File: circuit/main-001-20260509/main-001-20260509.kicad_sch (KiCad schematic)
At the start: 1 part, among them U1 DEV-16771

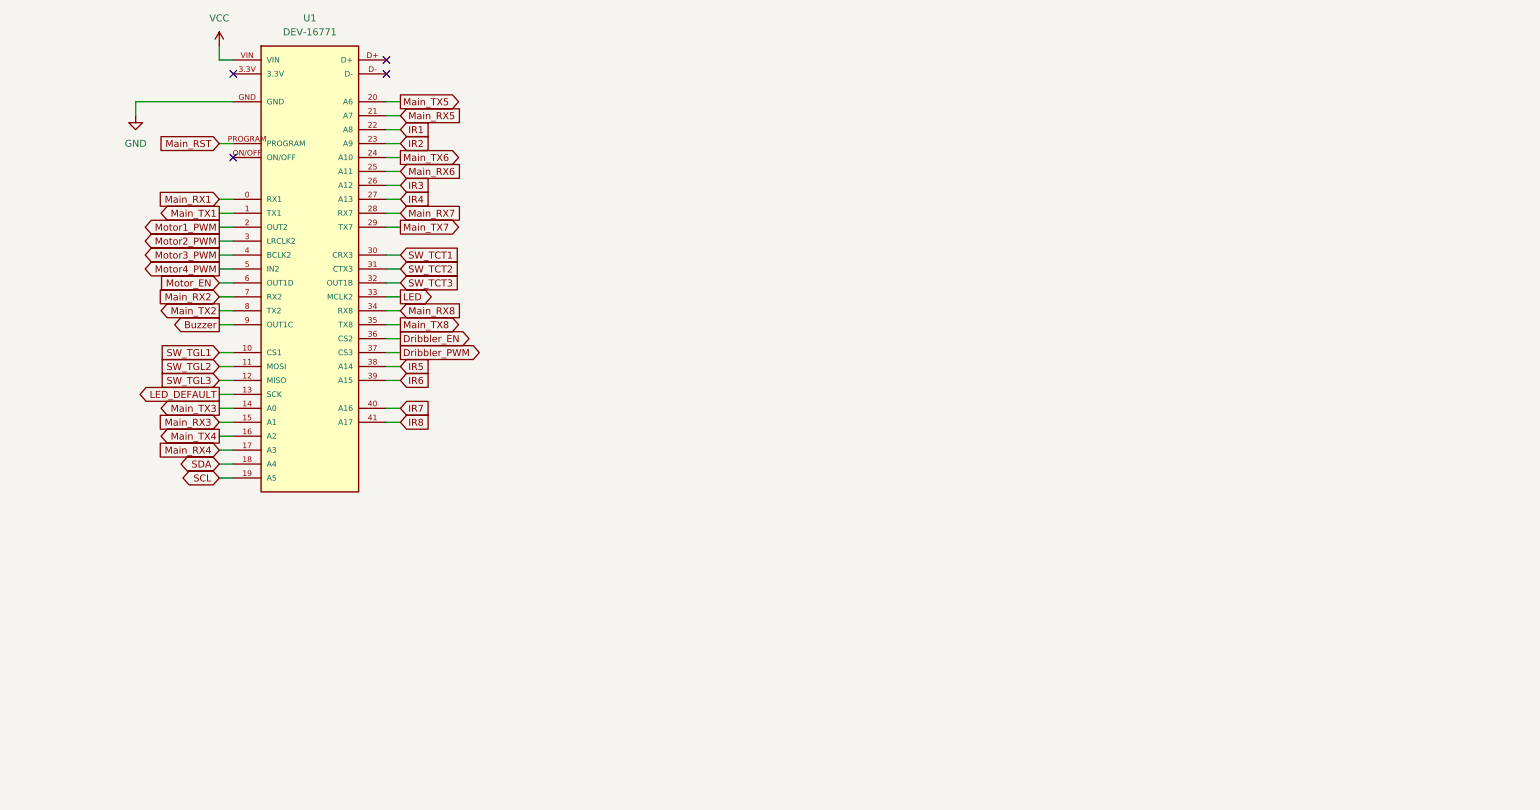
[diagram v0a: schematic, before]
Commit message: Update メイン基板の回路を進めた
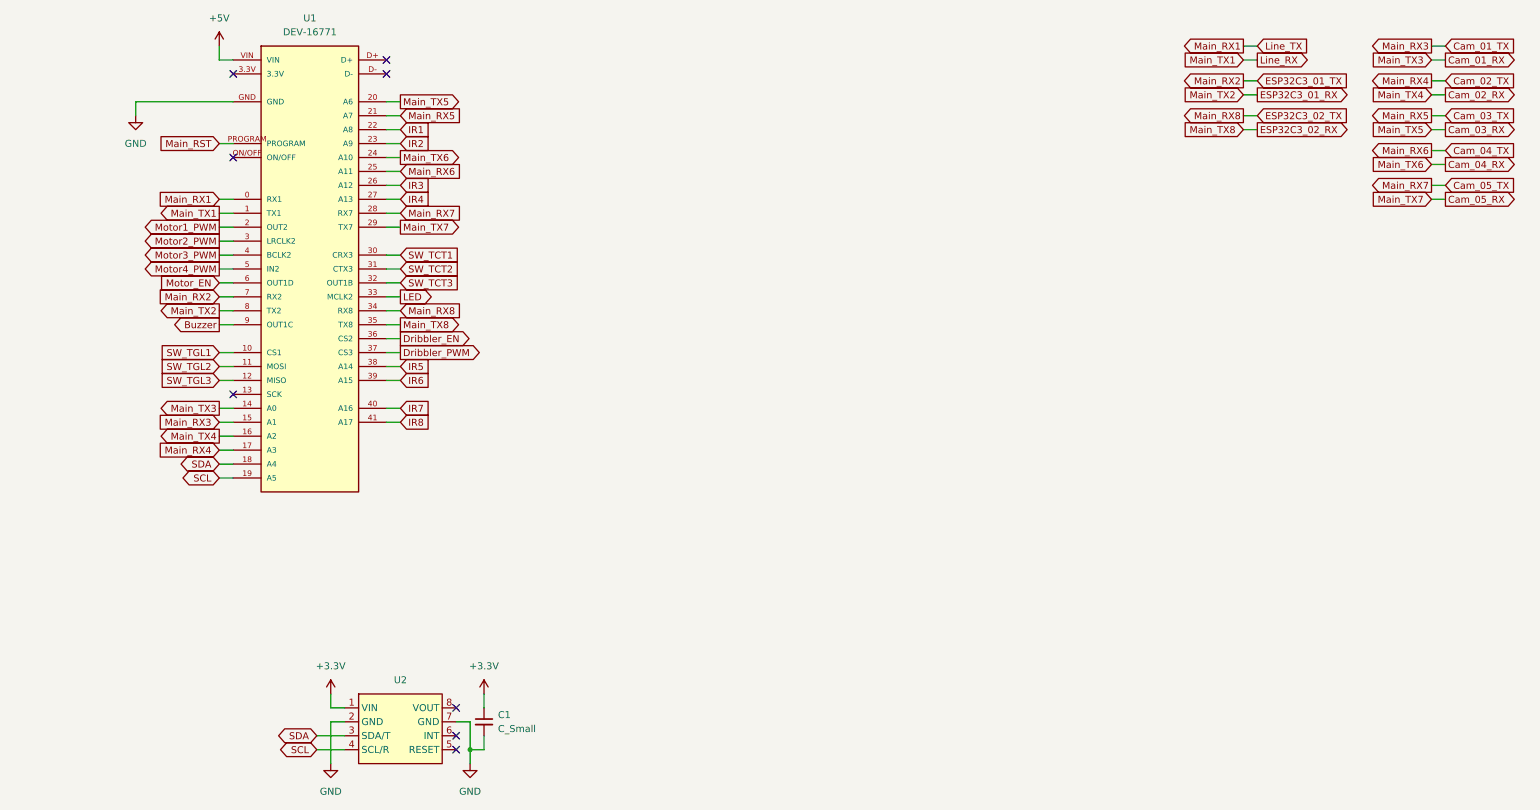
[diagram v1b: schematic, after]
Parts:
- added C1: C_Small, symbol Device:C_Small
- added U2: (no value), symbol @Thrive_symbol_main:BNO055
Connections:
- net GND: now also C1.2, U2.2 (GND), U2.7 (GND)
- net SCL: now also U2.4 (SCL/R)
- net SDA: now also U2.3 (SDA/T)
- net LED_DEFAULT: no longer names the net of U1.13 (SCK)
- net Main_RX1 renamed Line_TX
- net Main_RX2 renamed ESP32C3_01_TX
- net Main_RX3 renamed Cam_01_TX
- net Main_RX4 renamed Cam_02_TX
- net Main_RX5 renamed Cam_03_TX
- net Main_RX6 renamed Cam_04_TX
- net Main_RX7 renamed Cam_05_TX
- net Main_RX8 renamed ESP32C3_02_TX
- net Main_TX1 renamed Line_RX
- net Main_TX2 renamed ESP32C3_01_RX
- net Main_TX3 renamed Cam_01_RX
- net Main_TX4 renamed Cam_02_RX
- net Main_TX5 renamed Cam_03_RX
- net Main_TX6 renamed Cam_04_RX
- net Main_TX7 renamed Cam_05_RX
- net Main_TX8 renamed ESP32C3_02_RX
- net VCC renamed +5V
- new net +3.3V: C1.1, U2.1 (VIN)
- no-connect marks 4 -> 8

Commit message: Update メイン基板ほぼアップデートなし
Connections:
- net Line_TX: no longer U1.0 (RX1)
- new net RX1_{teensy}-TX_{Arduino}: U1.0 (RX1)
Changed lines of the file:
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@@
 		)
 	)
-	(global_label "Main_RX1"
+	(global_label "RX1_{teensy}-TX_{Arduino}"
 		(shape input)
 		(at 38.1 53.34 180)
@@
 		)
 		(property "Intersheetrefs" "${INTERSHEET_REFS}"
-			(at 25.8604 53.34 0)
+			(at 17.1268 53.34 0)
 			(hide yes)
 			(show_name no)

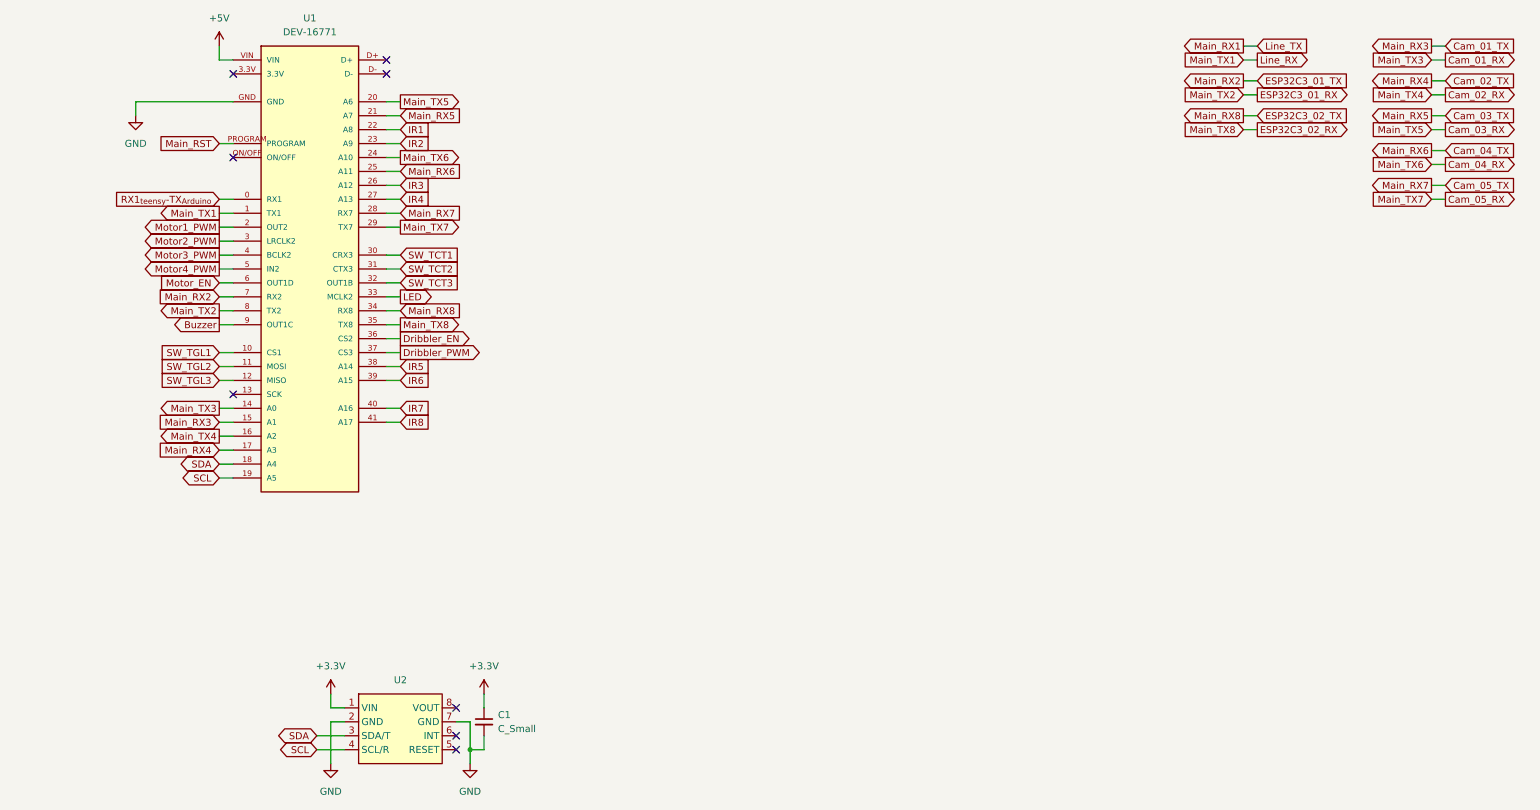
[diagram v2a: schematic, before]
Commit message: Update メイン基板はピン関連とレベル変換、サブ基板はESP周りを追加した
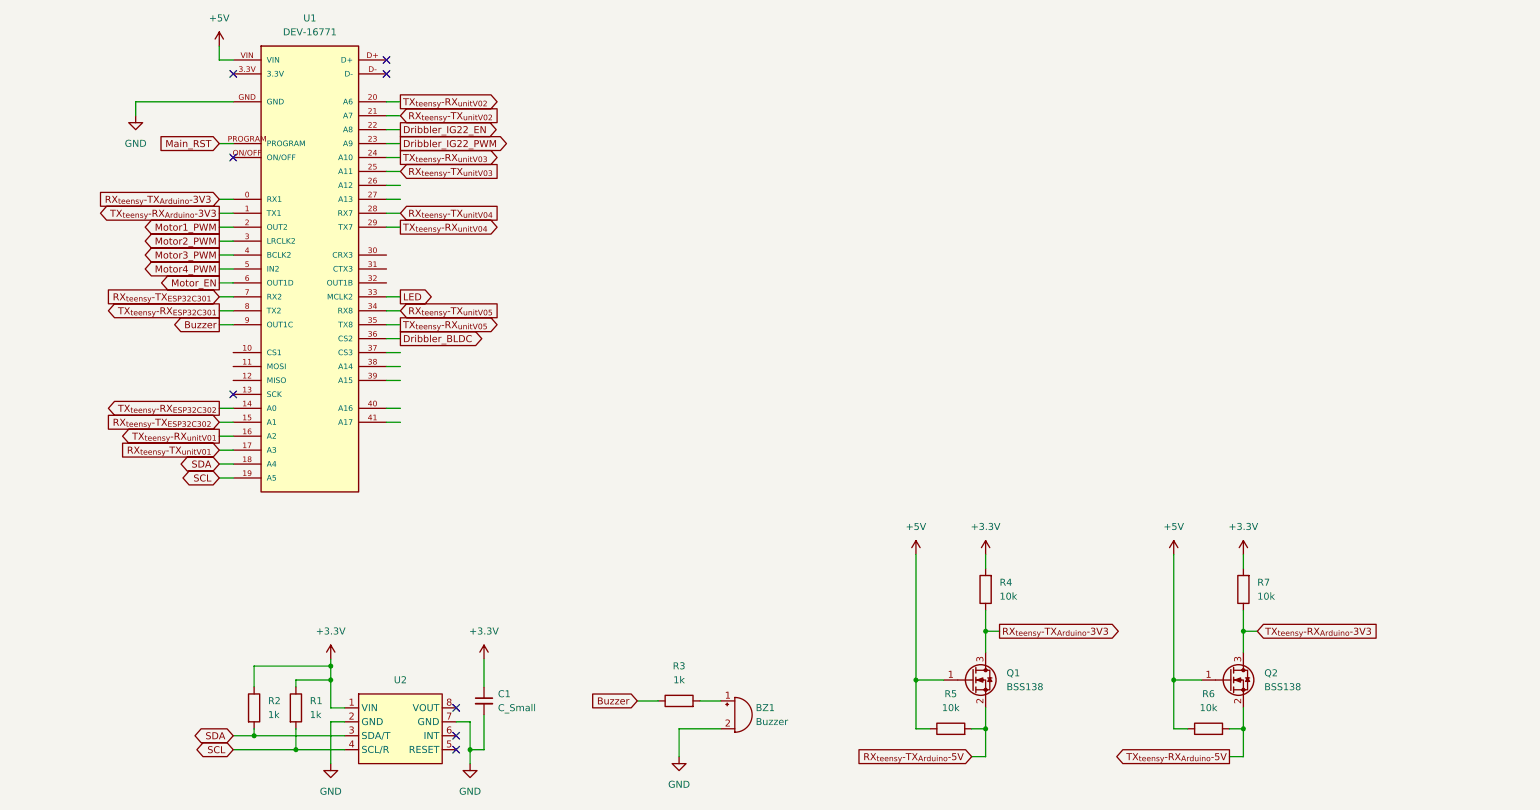
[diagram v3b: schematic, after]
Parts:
- added BZ1: Buzzer, symbol Device:Buzzer
- added Q1, Q2: BSS138, Package_TO_SOT_SMD:SOT-23, symbol Transistor_FET:BSS138
- added R1, R2, R3: 1k, symbol Device:R
- added R4, R5, R6, R7: 10k, symbol Device:R
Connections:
- net +3.3V: now also R1.1, R2.1, R4.2, R7.2
- net +5V: now also Q1.1 (G), Q2.1 (G), R5.1, R6.1
- net Buzzer: now also R3.1
- net GND: now also BZ1.2 (-)
- net SCL: now also R1.2
- net SDA: now also R2.2
- net Cam_01_RX renamed TX_{teensy}-RX_{ESP32C302}
- net Cam_01_TX renamed RX_{teensy}-TX_{ESP32C302}
- net Cam_02_RX renamed TX_{teensy}-RX_{unitV01}
- net Cam_02_TX renamed RX_{teensy}-TX_{unitV01}
- net Cam_03_RX renamed TX_{teensy}-RX_{unitV02}
- net Cam_03_TX renamed RX_{teensy}-TX_{unitV02}
- net Cam_04_RX renamed TX_{teensy}-RX_{unitV03}
- net Cam_04_TX renamed RX_{teensy}-TX_{unitV03}
- net Cam_05_RX renamed TX_{teensy}-RX_{unitV04}
- net Cam_05_TX renamed RX_{teensy}-TX_{unitV04}
- net Dribbler_EN renamed Dribbler_BLDC
- net Dribbler_PWM: no longer names the net of U1.37 (CS3)
- net ESP32C3_01_RX renamed TX_{teensy}-RX_{ESP32C301}
- net ESP32C3_01_TX renamed RX_{teensy}-TX_{ESP32C301}
- net ESP32C3_02_RX renamed TX_{teensy}-RX_{unitV05}
- net ESP32C3_02_TX renamed RX_{teensy}-TX_{unitV05}
- net IR1 renamed Dribbler_IG22_EN
- net IR2 renamed Dribbler_IG22_PWM
- net IR3: no longer names the net of U1.26 (A12)
- net IR4: no longer names the net of U1.27 (A13)
- net IR5: no longer names the net of U1.38 (A14)
- net IR6: no longer names the net of U1.39 (A15)
- net IR7: no longer names the net of U1.40 (A16)
- net IR8: no longer names the net of U1.41 (A17)
- net Line_RX renamed TX_{teensy}-RX_{Arduino}-3V3
- net TX_{teensy}-RX_{Arduino}-3V3: now also Q2.3 (D), R7.1
- net RX1_{teensy}-TX_{Arduino} renamed RX_{teensy}-TX_{Arduino}-3V3
- net RX_{teensy}-TX_{Arduino}-3V3: now also Q1.3 (D), R4.1
- net SW_TCT1: no longer names the net of U1.30 (CRX3)
- net SW_TCT2: no longer names the net of U1.31 (CTX3)
- net SW_TCT3: no longer names the net of U1.32 (OUT1B)
- net SW_TGL1: no longer names the net of U1.10 (CS1)
- net SW_TGL2: no longer names the net of U1.11 (MOSI)
- net SW_TGL3: no longer names the net of U1.12 (MISO)
- new net: BZ1.1 (+), R3.2
- new net RX_{teensy}-TX_{Arduino}-5V: Q1.2 (S), R5.2
- new net TX_{teensy}-RX_{Arduino}-5V: Q2.2 (S), R6.2
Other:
- moved on the sheet: C1

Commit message: Create ネオピクセル基板完成した
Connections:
- net ballcatchsig_front: now reaches U1.10 (CS1)
- net ballcatchsig_back: now reaches U1.11 (MOSI)
- net SW_TCT: now reaches U1.12 (MISO)
- net RX_{teensy}-TX_{unitV01} renamed RX_{teensy}-TX_{unitV1}
- net RX_{teensy}-TX_{unitV02} renamed RX_{teensy}-TX_{unitV2}
- net RX_{teensy}-TX_{unitV03} renamed RX_{teensy}-TX_{unitV3}
- net RX_{teensy}-TX_{unitV04} renamed RX_{teensy}-TX_{unitV4}
- net RX_{teensy}-TX_{unitV05} renamed RX_{teensy}-TX_{unitV5}
- net TX_{teensy}-RX_{unitV01} renamed TX_{teensy}-RX_{unitV1}
- net TX_{teensy}-RX_{unitV02} renamed TX_{teensy}-RX_{unitV2}
- net TX_{teensy}-RX_{unitV03} renamed TX_{teensy}-RX_{unitV3}
- net TX_{teensy}-RX_{unitV04} renamed TX_{teensy}-RX_{unitV4}
- net TX_{teensy}-RX_{unitV05} renamed TX_{teensy}-RX_{unitV5}
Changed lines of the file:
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@@
+	(wire
+		(pts
+			(xy 38.1 83.82) (xy 40.64 83.82)
+		)
+		(stroke
+			(width 0)
+			(type default)
+		)
+	)
 	(wire
 		(pts
@@
 	(wire
 		(pts
+			(xy 38.1 81.28) (xy 40.64 81.28)
+		)
+		(stroke
+			(width 0)
+			(type default)
+		)
+	)
+	(wire
+		(pts
+			(xy 38.1 86.36) (xy 40.64 86.36)
+		)
+		(stroke
+			(width 0)
+			(type default)
+		)
+	)
+	(wire
+		(pts
 			(xy 52.07 142.24) (xy 52.07 140.97)
 		)
@@
 		)
 	)
-	(global_label "RX_{teensy}-TX_{unitV05}"
+	(global_label "RX_{teensy}-TX_{unitV5}"
 		(shape input)
 		(at 71.12 73.66 0)
@@
 		)
 		(property "Intersheetrefs" "${INTERSHEET_REFS}"
-			(at 90.9321 73.66 0)
+			(at 89.9645 73.66 0)
 			(hide yes)
 			(show_name no)
@@
 		)
 	)
+	(global_label "ballcatchsig_back"
+		(shape input)
+		(at 38.1 83.82 180)
+		(fields_autoplaced yes)
+		(effects
+			(font
+				(size 1.27 1.27)
+			)
+			(justify right)
+		)
+		(property "Intersheetrefs" "${INTERSHEET_REFS}"
+			(at 18.1213 83.82 0)
+			(hide yes)
+			(show_name no)
+			(do_not_autoplace no)
+			(effects
+				(font
+					(size 1.27 1.27)
+				)
+				(justify right)
+			)
+		)
+	)
 	(global_label "Motor3_PWM"
 		(shape output)
@@
 		)
 	)
+	(global_label "ballcatchsig_front"
+		(shape input)
+		(at 38.1 81.28 180)
+		(fields_autoplaced yes)
+		(effects
+			(font
+				(size 1.27 1.27)
+			)
+			(justify right)
+		)
+		(property "Intersheetrefs" "${INTERSHEET_REFS}"
+			(at 18.0004 81.28 0)
+			(hide yes)
+			(show_name no)
+			(do_not_autoplace no)
+			(effects
+				(font
+					(size 1.27 1.27)
+				)
+				(justify right)
+			)
+		)
+	)
 	(global_label "RX_{teensy}-TX_{ESP32C301}"
 		(shape input)
@@
 		)
 	)
-	(global_label "RX_{teensy}-TX_{unitV02}"
+	(global_label "RX_{teensy}-TX_{unitV2}"
 		(shape input)
 		(at 71.12 38.1 0)
@@
 		)
 		(property "Intersheetrefs" "${INTERSHEET_REFS}"
-			(at 90.9321 38.1 0)
+			(at 89.9645 38.1 0)
 			(hide yes)
 			(show_name no)
@@
 		)
 	)
-	(global_label "RX_{teensy}-TX_{unitV03}"
+	(global_label "RX_{teensy}-TX_{unitV3}"
 		(shape input)
 		(at 71.12 48.26 0)
@@
 		)
 		(property "Intersheetrefs" "${INTERSHEET_REFS}"
-			(at 90.9321 48.26 0)
+			(at 89.9645 48.26 0)
 			(hide yes)
 			(show_name no)
@@
 		)
 	)
-	(global_label "RX_{teensy}-TX_{unitV01}"
+	(global_label "RX_{teensy}-TX_{unitV1}"
 		(shape input)
 		(at 38.1 99.06 180)
@@
 		)
 		(property "Intersheetrefs" "${INTERSHEET_REFS}"
-			(at 18.2879 99.06 0)
+			(at 19.2555 99.06 0)
 			(hide yes)
 			(show_name no)
@@
 		)
 	)
-	(global_label "RX_{teensy}-TX_{unitV04}"
+	(global_label "RX_{teensy}-TX_{unitV4}"
 		(shape input)
 		(at 71.12 55.88 0)
@@
 		)
 		(property "Intersheetrefs" "${INTERSHEET_REFS}"
-			(at 90.9321 55.88 0)
+			(at 89.9645 55.88 0)
 			(hide yes)
 			(show_name no)
@@
 		)
 	)
-	(global_label "TX_{teensy}-RX_{unitV05}"
+	(global_label "TX_{teensy}-RX_{unitV5}"
 		(shape output)
 		(at 71.12 76.2 0)
@@
 		)
 		(property "Intersheetrefs" "${INTERSHEET_REFS}"
-			(at 90.9321 76.2 0)
+			(at 89.9645 76.2 0)
 			(hide yes)
 			(show_name no)
@@
 		)
 	)
-	(global_label "TX_{teensy}-RX_{unitV01}"
+	(global_label "TX_{teensy}-RX_{unitV1}"
 		(shape output)
 		(at 38.1 96.52 180)
@@
 		)
 		(property "Intersheetrefs" "${INTERSHEET_REFS}"
-			(at 18.2879 96.52 0)
+			(at 19.2555 96.52 0)
 			(hide yes)
 			(show_name no)
@@
 		)
 	)
-	(global_label "TX_{teensy}-RX_{unitV04}"
+	(global_label "TX_{teensy}-RX_{unitV4}"
 		(shape output)
 		(at 71.12 58.42 0)
@@
 		)
 		(property "Intersheetrefs" "${INTERSHEET_REFS}"
-			(at 90.9321 58.42 0)
+			(at 89.9645 58.42 0)
 			(hide yes)
 			(show_name no)
@@
 		)
 	)
-	(global_label "TX_{teensy}-RX_{unitV03}"
+	(global_label "TX_{teensy}-RX_{unitV3}"
 		(shape output)
 		(at 71.12 45.72 0)
@@
 		)
 		(property "Intersheetrefs" "${INTERSHEET_REFS}"
-			(at 90.9321 45.72 0)
+			(at 89.9645 45.72 0)
 			(hide yes)
 			(show_name no)
@@
 		)
 	)
-	(global_label "TX_{teensy}-RX_{unitV02}"
+	(global_label "TX_{teensy}-RX_{unitV2}"
 		(shape output)
 		(at 71.12 35.56 0)
@@
 		)
 		(property "Intersheetrefs" "${INTERSHEET_REFS}"
-			(at 90.9321 35.56 0)
+			(at 89.9645 35.56 0)
 			(hide yes)
 			(show_name no)
@@
 			(hide yes)
 			(show_name no)
+			(do_not_autoplace no)
+			(effects
+				(font
+					(size 1.27 1.27)
+				)
+				(justify right)
+			)
+		)
+	)
+	(global_label "SW_TCT"
+		(shape input)
+		(at 38.1 86.36 180)
+		(fields_autoplaced yes)
+		(effects
+			(font
+				(size 1.27 1.27)
+			)
+			(justify right)
+		)
+		(property "Intersheetrefs" "${INTERSHEET_REFS}"
+			(at 28.2811 86.36 0)
+			(hide yes)
+			(show_name no)
